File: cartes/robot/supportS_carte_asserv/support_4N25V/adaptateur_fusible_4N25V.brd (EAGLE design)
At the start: 32.1 x 31.7 mm, 16 parts

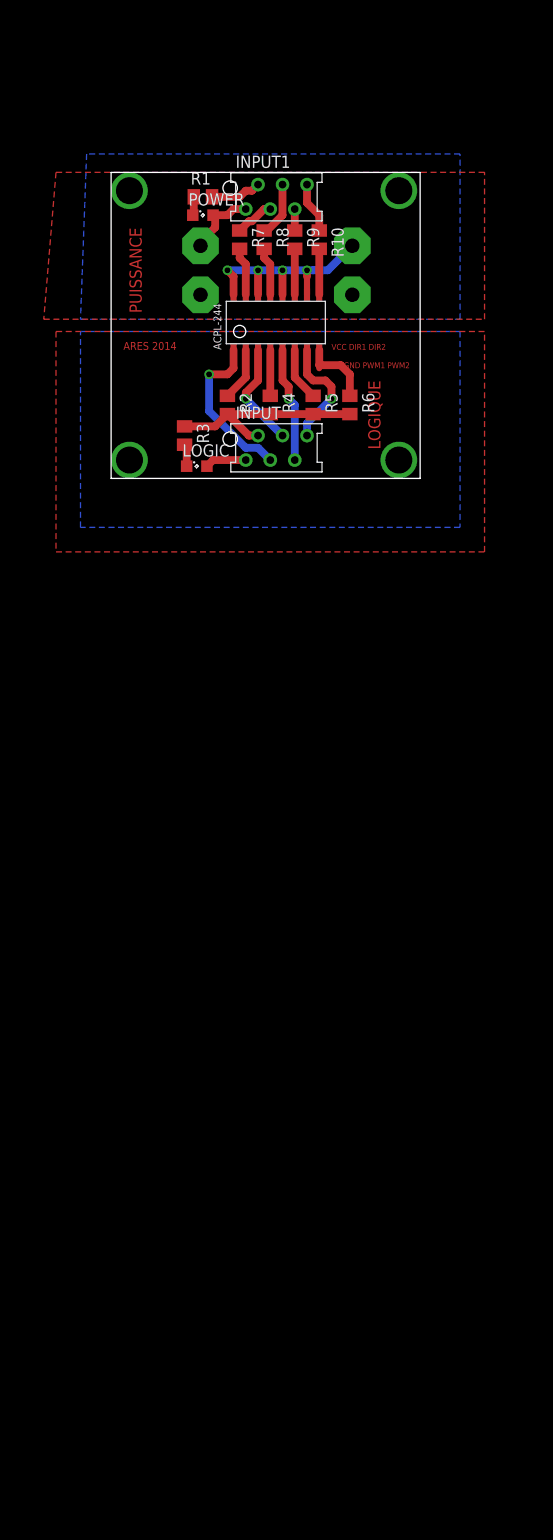
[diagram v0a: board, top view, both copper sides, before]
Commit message: Ajout nvlle carte opto
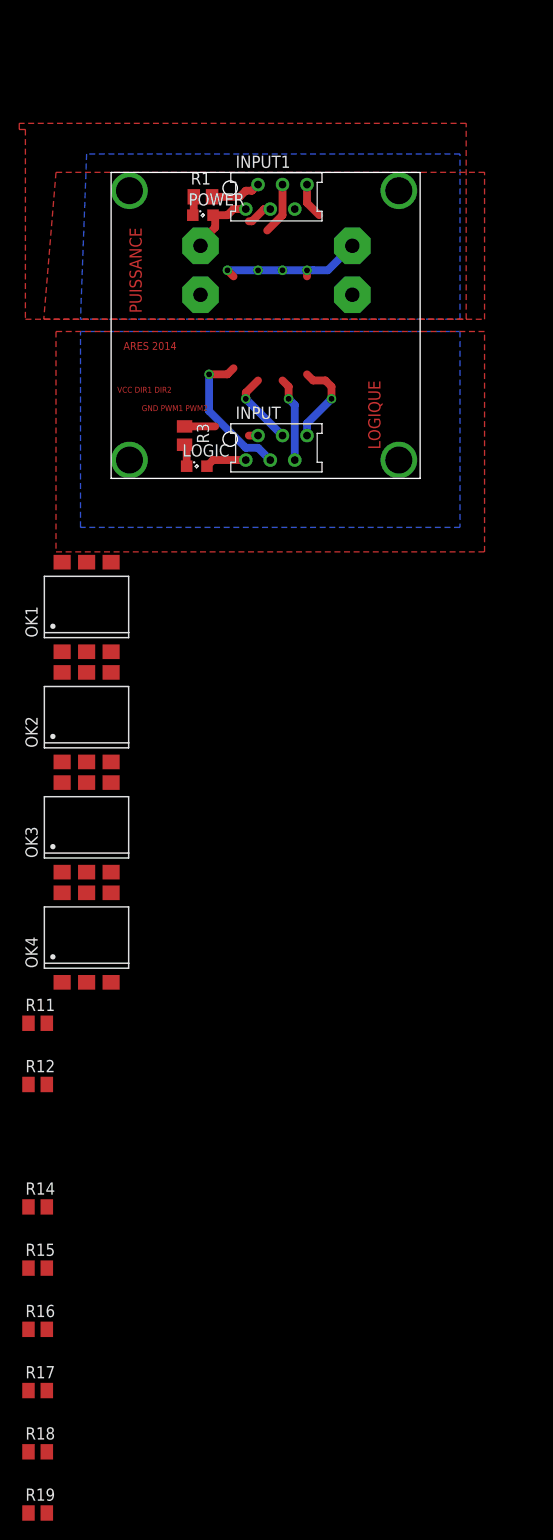
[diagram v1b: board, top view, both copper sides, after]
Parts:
- removed R10, R7, R8, R9: 470, rcl:M0805
- removed R2, R4, R5, R6: 1k, rcl:M0805
- removed U$1: ACPL-244, acpl-244:ACPL-244
- added OK1, OK2, OK3, OK4: 4N25SM, optocoupler:DIL6-SMD
- added R11, R12, R14, R15: 1k, rcl:M0805
- added R16, R17, R18, R19: 470, rcl:M0805
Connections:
- removed net N$11: R5.1, U$1.6
- removed net N$12: R6.1, U$1.8
- removed net N$13: R7.2, U$1.15
- removed net N$14: R8.2, U$1.13
- removed net N$16: R10.2, U$1.9
- new net N$19: OK1.4, R16.2
- new net N$20: OK2.4, R17.2
- new net N$21: OK3.4, R18.2
- new net N$22: OK4.4, R19.2
- new net N$9: OK3.2, R14.1
- net C_DIR1: no longer U$1.1
- net C_DIR2: now also OK3.1; no longer U$1.5
- net C_PWM1: now also OK2.1; no longer U$1.3
- net C_PWM2: now also OK4.1; no longer U$1.7
- net DIR1: now also R16.1; no longer R7.1
- net DIR2: now also R18.1; no longer R9.1
- net FUSE_5V: no longer U$1.10, U$1.12, U$1.14, U$1.16
- net GND: now also R11.2, R12.2, R14.2, R15.2; no longer R2.2, R4.2, R5.2, R6.2
- net N$1: now also OK1.2, R11.1; no longer R9.2, U$1.11
- net N$10: now also OK4.2, R15.1; no longer R4.1, U$1.4
- net N$2: now also OK2.2, R12.1; no longer R2.1, U$1.2
- net PWM1: now also R17.1; no longer R8.1
- net PWM2: now also R19.1; no longer R10.1
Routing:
- net GND: track 21.8 -> 4.12 mm
- net N$12: track 7.38 -> 0.00 mm
- net FUSE_5V: track 22.5 -> 15.5 mm
- net N$2: track 5.55 -> 0.00 mm
- net N$11: track 5.55 -> 0.00 mm
- net N$14: track 5.03 -> 0.00 mm
- net N$13: track 5.03 -> 0.00 mm
- net N$16: track 4.77 -> 0.00 mm
- net N$10: track 4.77 -> 0.00 mm
- net N$1: track 4.77 -> 0.00 mm
- net C_PWM1: track 11.0 -> 7.82 mm
- net C_DIR2: track 12.0 -> 8.78 mm
- net C_PWM2: track 11.7 -> 9.20 mm
- net DIR2: track 2.23 -> 0.00 mm
- net C_DIR1: track 17.0 -> 15.1 mm
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
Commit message: nouvelle carte sans ne555
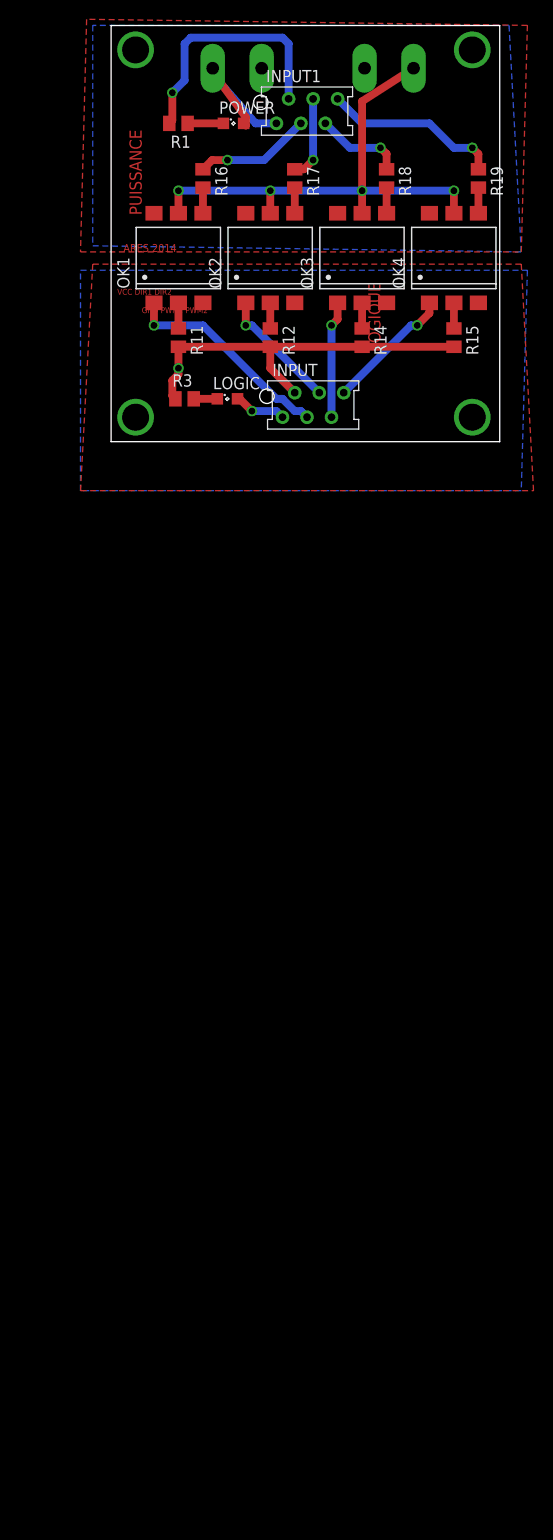
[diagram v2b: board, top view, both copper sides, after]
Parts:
- F3: device fuse:SHK20Q -> fuse:SHK20L
- moved R19 145.8 mm to (41.3, 31.1), turned to 270 degrees
- moved R18 136.9 mm to (31.8, 31.1), turned to 270 degrees
- moved R17 128.5 mm to (22.2, 31.1), turned to 270 degrees
- moved R16 120.6 mm to (12.7, 31.1), turned to 270 degrees
- moved R15 105.7 mm to (38.7, 14.6), turned to 270 degrees
- moved R14 96.2 mm to (29.2, 14.6), turned to 270 degrees
- moved R12 81.1 mm to (19.7, 14.6), turned to 270 degrees
- moved OK4 80.1 mm to (38.7, 22.9)
- moved R11 72.6 mm to (10.2, 14.6), turned to 270 degrees
- moved OK3 65.6 mm to (29.2, 22.9)
- moved OK2 51.3 mm to (19.7, 22.9)
- moved OK1 37.4 mm to (10.2, 22.9)
- moved F3 21.3 mm to (24.1, 42.5)
- moved POWER 10.0 mm to (15.9, 36.8)
- moved INPUT1 9.44 mm to (20.3, 36.8)
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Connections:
- net C_DIR1: now also OK1.1
- net FUSE_5V: now also OK1.5, OK2.5, OK3.5, OK4.5
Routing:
- net FUSE_5V: track 15.5 -> 53.5 mm
- net GND: track 4.12 -> 42.0 mm, vias 0 -> 1
- net GNDA: track 5.29 -> 25.9 mm, vias 0 -> 1
- net PWM2: track 3.70 -> 18.6 mm, vias 0 -> 1
- net DIR1: track 2.75 -> 12.1 mm, vias 0 -> 1
- net +5V: track 7.56 -> 16.9 mm
- net DIR2: track 0.00 -> 9.26 mm, vias 0 -> 1
- net C_DIR1: track 15.1 -> 22.2 mm
- net C_PWM1: track 7.82 -> 12.9 mm
- net C_PWM2: track 9.20 -> 13.4 mm
- net C_DIR2: track 8.78 -> 12.1 mm
- net PWM1: track 5.42 -> 8.65 mm, vias 0 -> 1
- net N$9: track 0.00 -> 2.66 mm
- net N$22: track 0.00 -> 2.66 mm
- net N$21: track 0.00 -> 2.66 mm
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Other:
- board size 32.1 x 31.7 mm -> 40.3 x 43.2 mm
